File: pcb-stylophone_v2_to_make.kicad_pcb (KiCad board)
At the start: 2 copper layers, 85.6 x 54 mm, 48 parts, among them J1 Batt, J10 Key 9, J11 Key 10, J12 Key 11, J13 Key 12, J14 Key 13, J15 Key 14, J16 Key 15, J17 Key 16, J18 Key 17, J19 Key 18, J2 Key 1, J20 Key 19, J21 Key 20, J22 Stylus, J3 Key 2, J4 Key 3, J5 Key 4, J6 Key 5, J7 Key 6, J8 Key 7, J9 Key 8, U1 NE555P

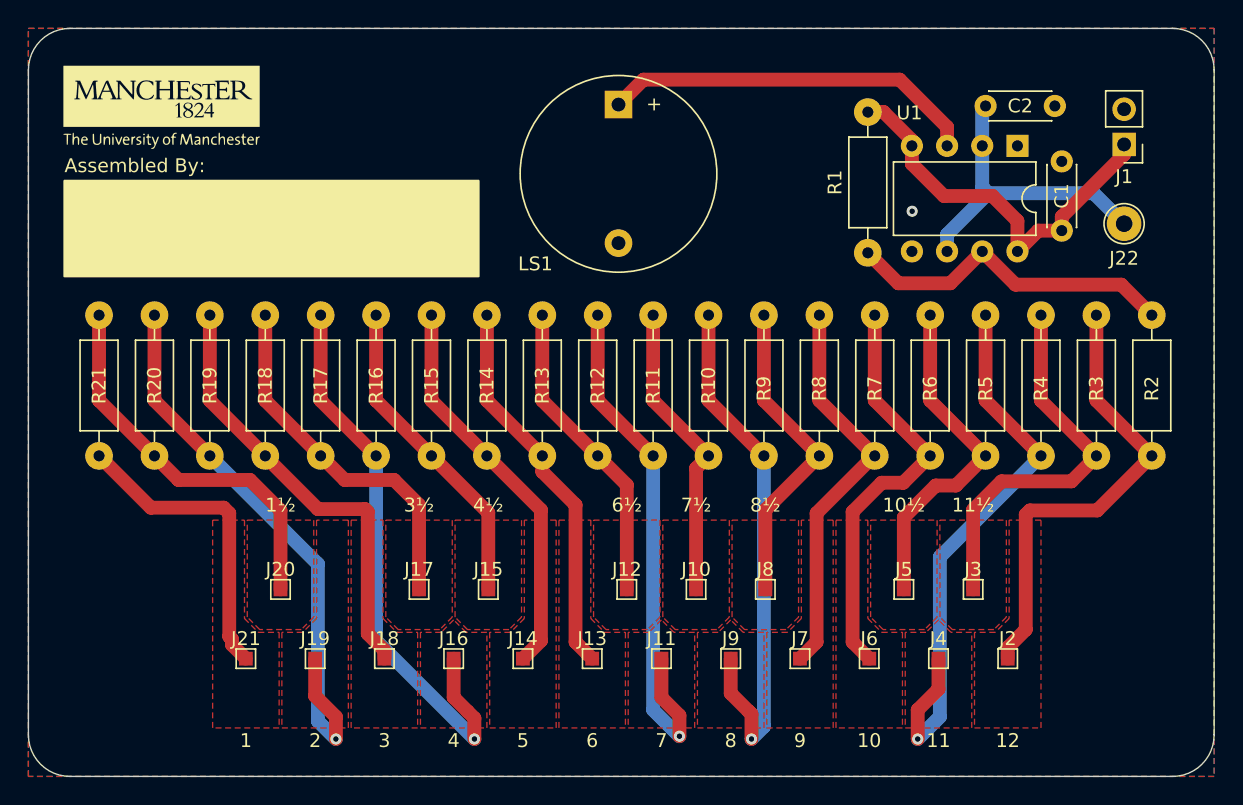
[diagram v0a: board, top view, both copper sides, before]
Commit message: stylophone v2 has bigger resistor soldering pads
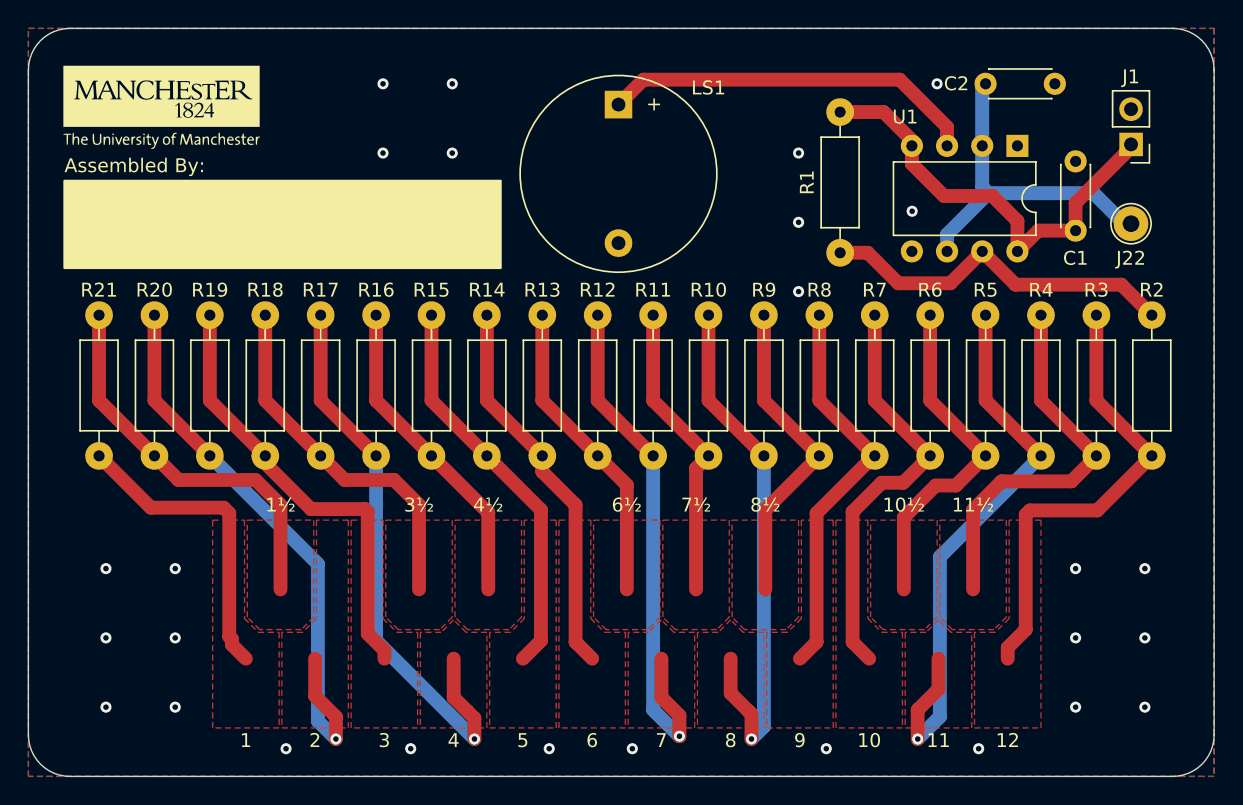
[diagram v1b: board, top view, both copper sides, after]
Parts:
- removed J10: Key 9, TestPoint:TestPoint_Pad_1.0x1.0mm
- removed J11: Key 10, TestPoint:TestPoint_Pad_1.0x1.0mm
- removed J12: Key 11, TestPoint:TestPoint_Pad_1.0x1.0mm
- removed J13: Key 12, TestPoint:TestPoint_Pad_1.0x1.0mm
- removed J14: Key 13, TestPoint:TestPoint_Pad_1.0x1.0mm
- removed J15: Key 14, TestPoint:TestPoint_Pad_1.0x1.0mm
- removed J16: Key 15, TestPoint:TestPoint_Pad_1.0x1.0mm
- removed J17: Key 16, TestPoint:TestPoint_Pad_1.0x1.0mm
- removed J18: Key 17, TestPoint:TestPoint_Pad_1.0x1.0mm
- removed J19: Key 18, TestPoint:TestPoint_Pad_1.0x1.0mm
- removed J2: Key 1, TestPoint:TestPoint_Pad_1.0x1.0mm
- removed J20: Key 19, TestPoint:TestPoint_Pad_1.0x1.0mm
- removed J21: Key 20, TestPoint:TestPoint_Pad_1.0x1.0mm
- removed J3: Key 2, TestPoint:TestPoint_Pad_1.0x1.0mm
- removed J4: Key 3, TestPoint:TestPoint_Pad_1.0x1.0mm
- removed J5: Key 4, TestPoint:TestPoint_Pad_1.0x1.0mm
- removed J6: Key 5, TestPoint:TestPoint_Pad_1.0x1.0mm
- removed J7: Key 6, TestPoint:TestPoint_Pad_1.0x1.0mm
- removed J8: Key 7, TestPoint:TestPoint_Pad_1.0x1.0mm
- removed J9: Key 8, TestPoint:TestPoint_Pad_1.0x1.0mm
- moved R1 2.00 mm to (143.0, 112.2)
- moved C2 1.60 mm to (153.5, 100.0)
- moved C1 1.00 mm to (160.0, 110.6)
- moved J1 0.50 mm to (164.0, 104.4)
- moved J22 0.50 mm to (164.0, 110.1)
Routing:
- net VCC: track 29.2 -> 32.0 mm
- net Net-(J22-Pin_1): track 22.7 -> 24.8 mm
- net Net-(U1-DIS): track 24.3 -> 26.3 mm
- net GND: vias 1 -> 27
